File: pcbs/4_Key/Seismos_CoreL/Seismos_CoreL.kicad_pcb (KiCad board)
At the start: 2 copper layers, 147 x 78 mm, 27 parts, among them J1 SM09B-SRSS-TB(LF)(SN), J2 SM09B-SRSS-TB(LF)(SN), J3 SM09B-SRSS-TB(LF)(SN), J4 SM09B-SRSS-TB(LF)(SN), J5 SM09B-SRSS-TB(LF)(SN), J6 SM09B-SRSS-TB(LF)(SN), J7 Conn_01x05_Pin, J8 MJ-4PP-9-Lily58, J9 SM09B-SRSS-TB(LF)(SN), SW1 RotaryEncoder_Switch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

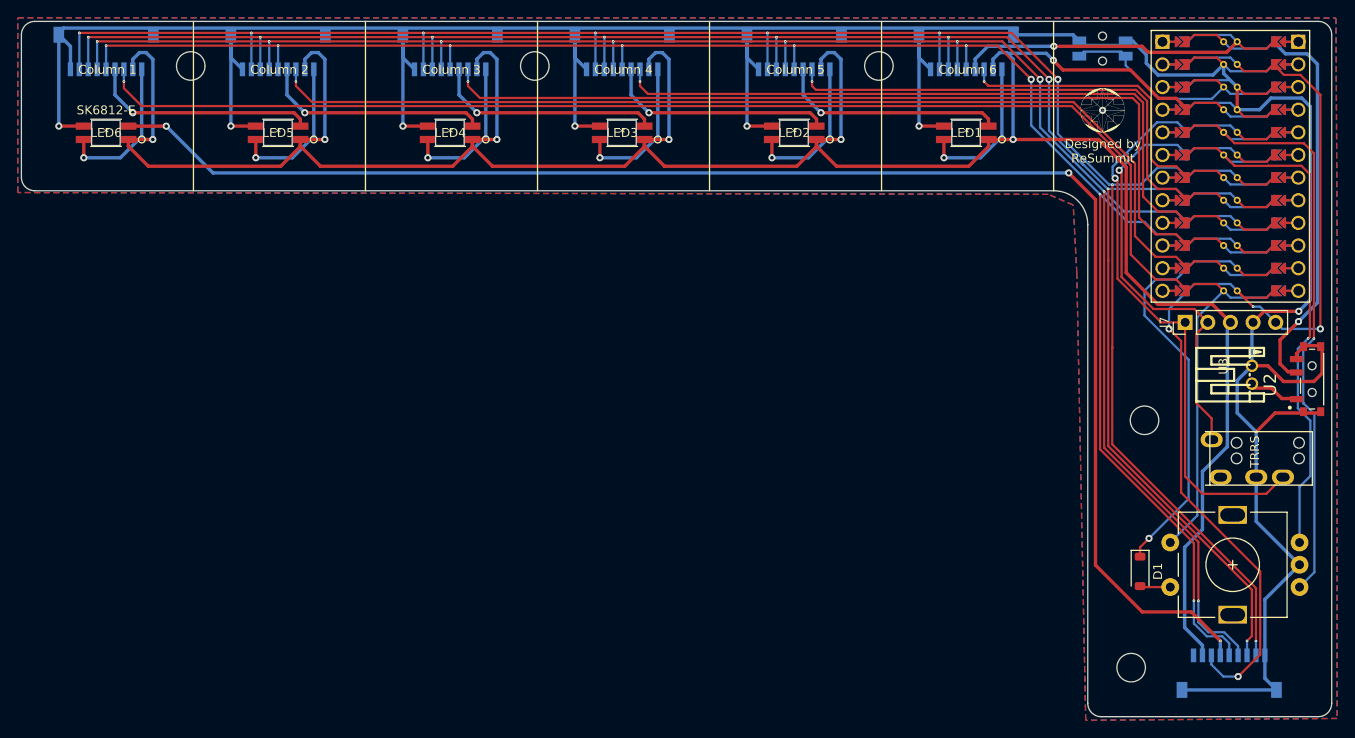
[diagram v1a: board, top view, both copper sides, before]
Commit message: Replaced microvias with very small vias
Also added small JLCJLCJLCJLC text for JLCPCB.

JLCPCB doesn't allow for blind microvias... so annoyingly I had to
reroute the row and column wiring. Luckily the 4 key doesn't use
microvias so that one is okay.
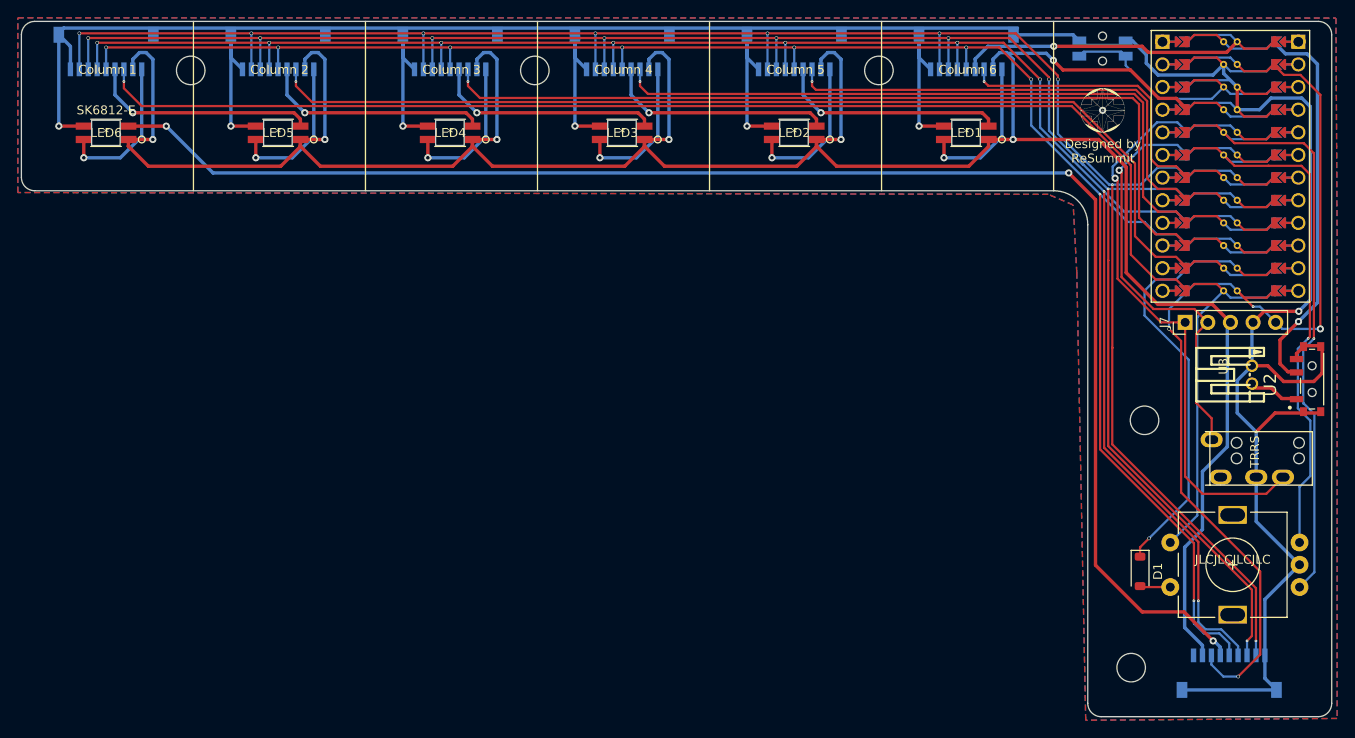
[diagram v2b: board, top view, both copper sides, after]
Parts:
- moved 2 0.50 mm to (87.6, 25.5)
- moved 4 0.50 mm to (126.2, 25.5)
- moved ? 0.50 mm to (49.0, 25.5)
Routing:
- net /Row4: track 208.3 -> 207.0 mm
- net /Row3: track 212.0 -> 211.1 mm
- net /Row2: track 215.2 -> 214.6 mm
- net /Row1: track 220.2 -> 220.7 mm
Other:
- board text added: "JLCJLCJLCJLC"

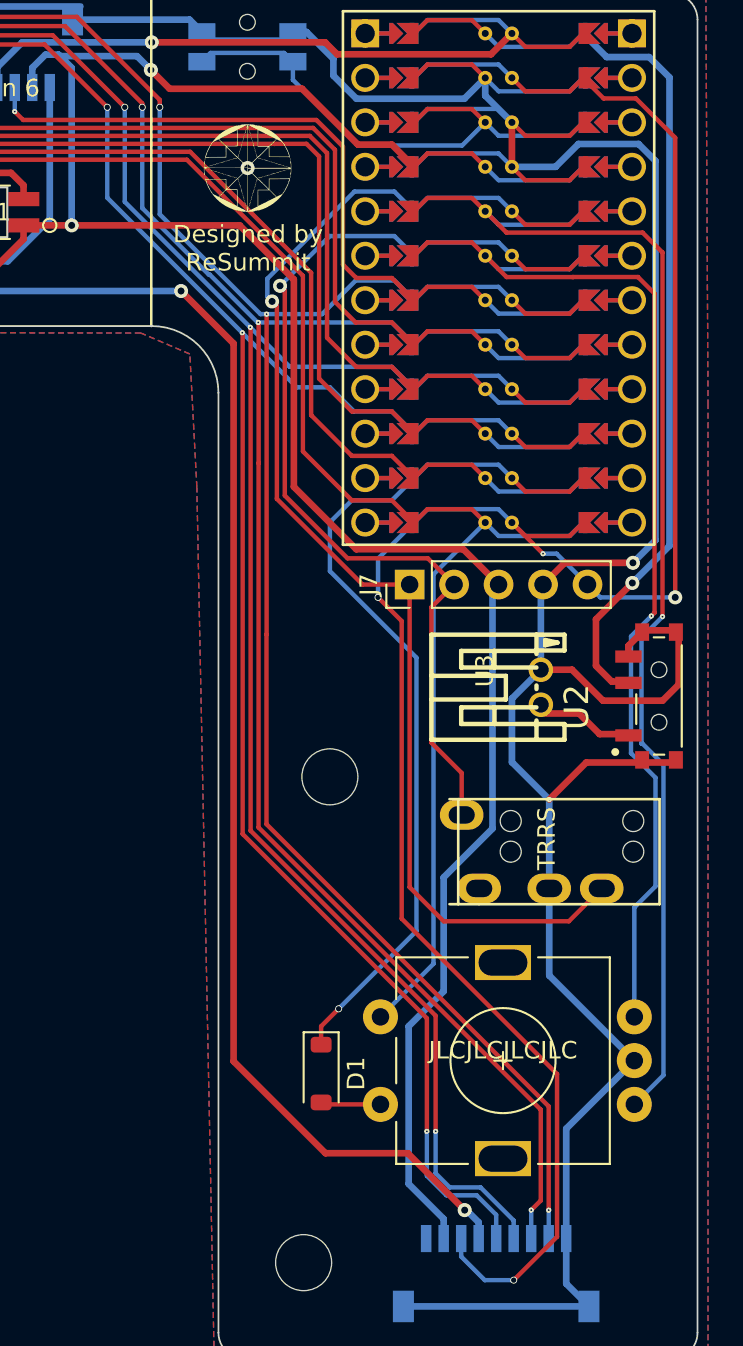
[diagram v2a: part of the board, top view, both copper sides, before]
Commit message: Replaced microvias in CoreL
I happened to find more... in CoreL only. CoreR looks mostly fine.
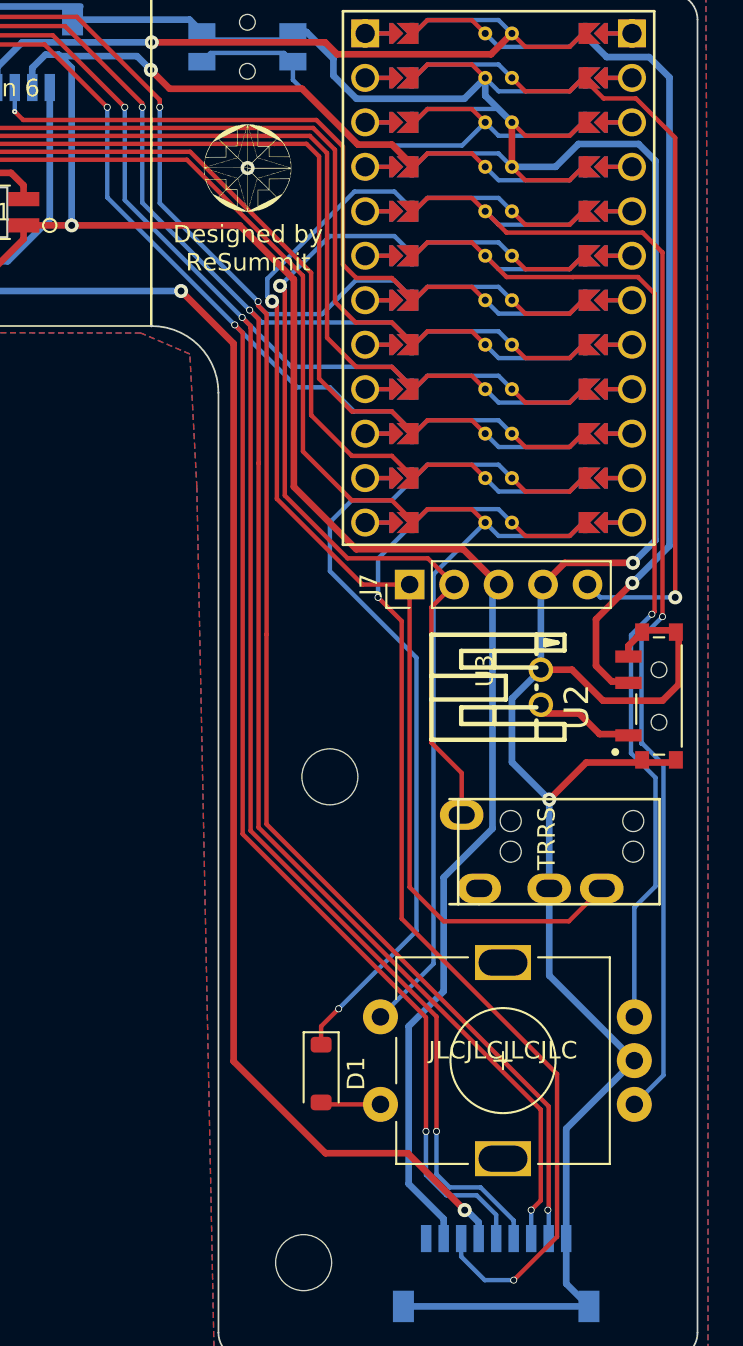
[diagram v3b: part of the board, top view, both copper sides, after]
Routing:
- net CS: track 44.0 -> 38.3 mm, vias 2 -> 1
- net /Row2: track 214.6 -> 215.4 mm
- net /Row1: track 220.7 -> 221.5 mm
- net /Row3: track 211.1 -> 211.8 mm
- net /Row4: track 207.0 -> 207.7 mm

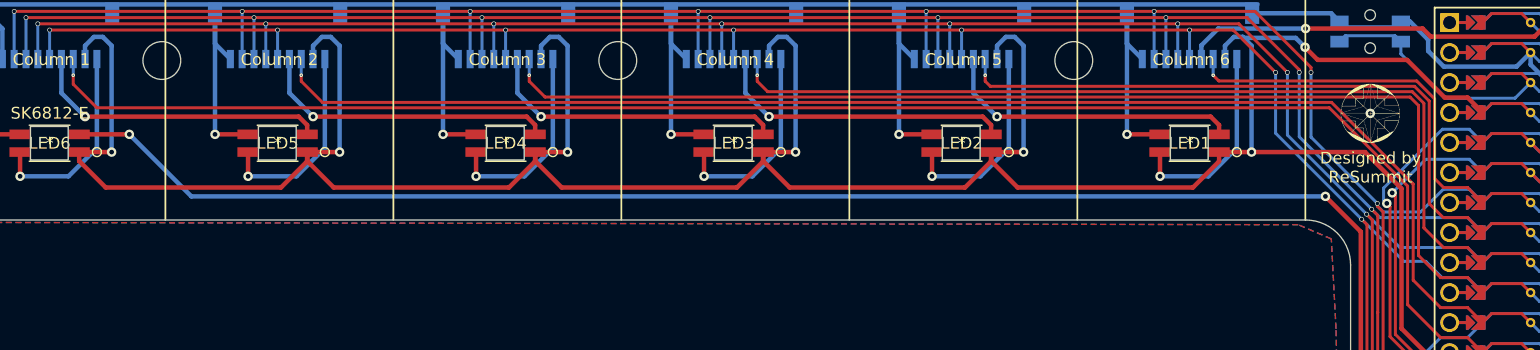
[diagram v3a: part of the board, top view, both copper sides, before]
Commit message: Last look over CoreL and removed microvias
CoreR has been verified by JLCPCB and is good to go. I forgot to add
teardrops to it so it is now added. CoreL on the other hand had some
more microvias near the JST SH conectors and under the rotary
encoder. These have been removed.

NOTE: Due to the microvia conversion, the previous commit was when the
NTPH holes near the columns have been shifted down by 0.5 mm. This will
be reflected in the case shortly but not yet as of now.

We'll see what JLCPCB says but it looks okay; hopefully I will get
results in a week or so.
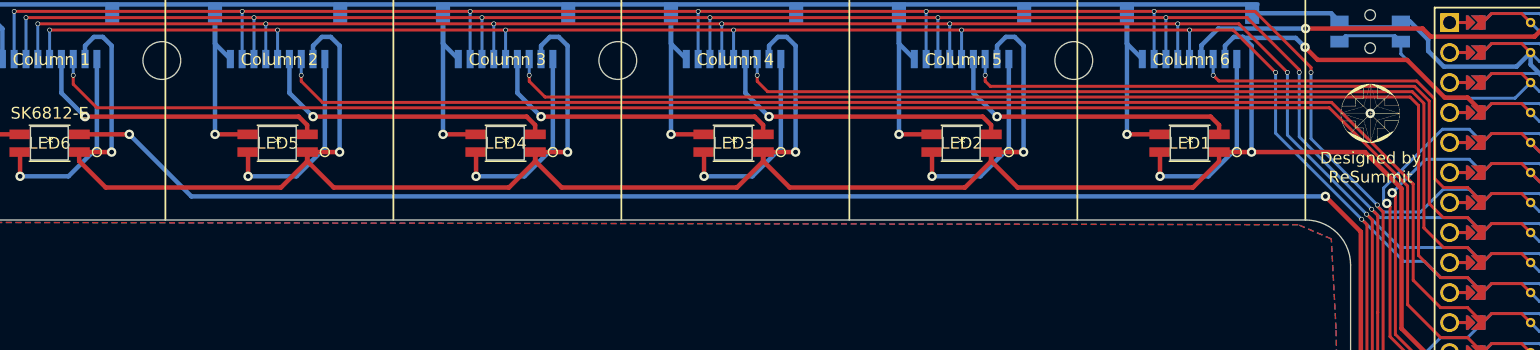
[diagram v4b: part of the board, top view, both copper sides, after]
